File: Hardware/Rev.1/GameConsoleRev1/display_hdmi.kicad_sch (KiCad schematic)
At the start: 11 parts, among them J7 HDMI_A

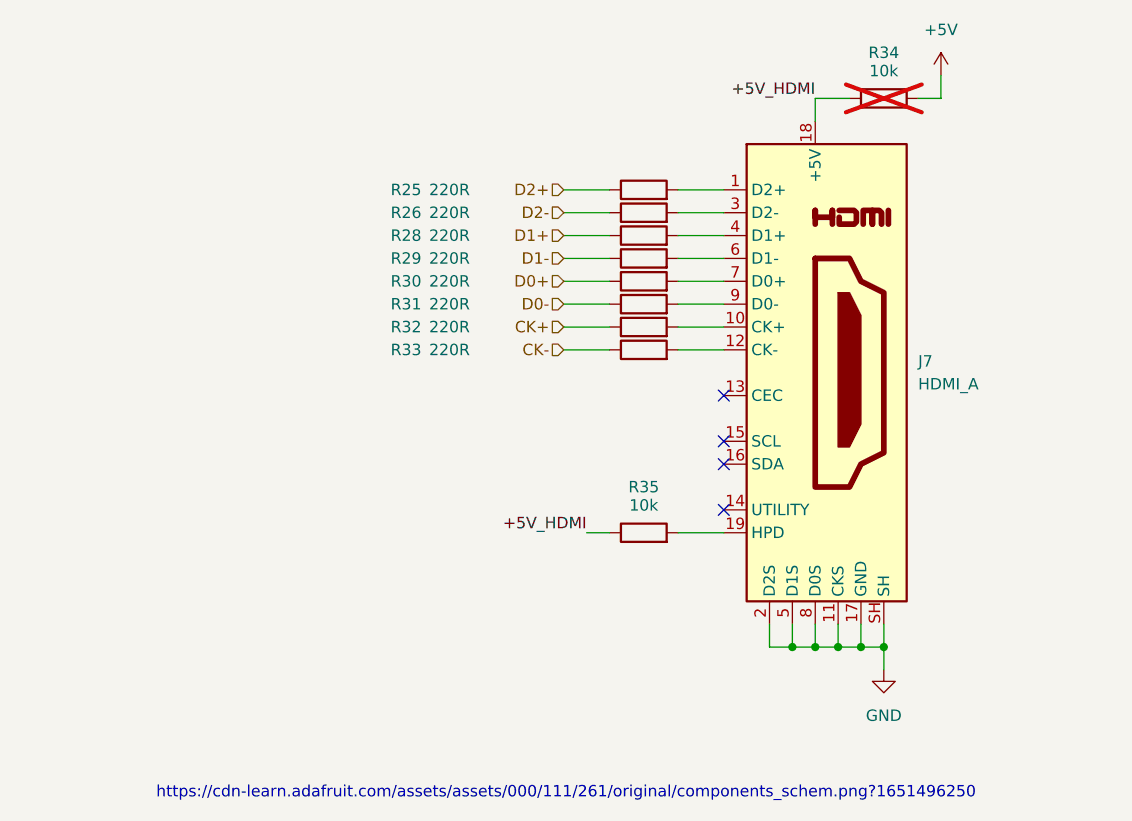
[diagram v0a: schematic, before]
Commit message: Added CPP Build
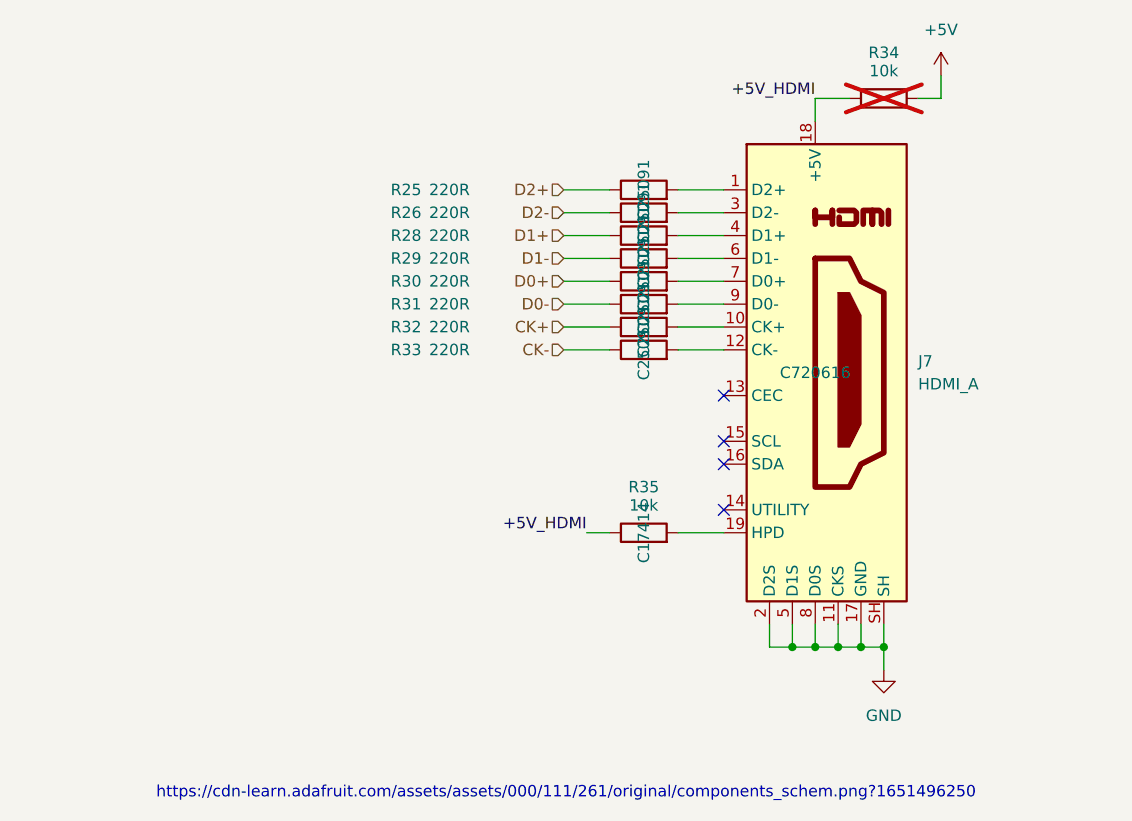
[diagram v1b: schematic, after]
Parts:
- J7: LCSC (none) -> C720616
- R25, R26, R28, R29, R30, R31, R32, R33: LCSC (none) -> C25091
- R35: LCSC (none) -> C17414
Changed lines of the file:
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@@
+			)
+		)
+		(property "DK" ""
+			(at 140.97 53.34 0)
+			(effects
+				(font
+					(size 1.27 1.27)
+				)
 			)
 		)
@@
 			)
 		)
+		(property "DK" ""
+			(at 114.3 71.12 0)
+			(effects
+				(font
+					(size 1.27 1.27)
+				)
+			)
+		)
+		(property "LCSC" "C25091"
+			(at 114.3 71.12 0)
+			(effects
+				(font
+					(size 1.27 1.27)
+				)
+			)
+		)
 		(pin "1"
 		)
@@
 			)
 		)
+		(property "DK" ""
+			(at 114.3 68.58 0)
+			(effects
+				(font
+					(size 1.27 1.27)
+				)
+			)
+		)
+		(property "LCSC" "C25091"
+			(at 114.3 68.58 0)
+			(effects
+				(font
+					(size 1.27 1.27)
+				)
+			)
+		)
 		(pin "1"
 		)
@@
 			)
 		)
+		(property "DK" ""
+			(at 114.3 66.04 0)
+			(effects
+				(font
+					(size 1.27 1.27)
+				)
+			)
+		)
+		(property "LCSC" "C25091"
+			(at 114.3 66.04 0)
+			(effects
+				(font
+					(size 1.27 1.27)
+				)
+			)
+		)
 		(pin "1"
 		)
@@
 			)
 		)
+		(property "DK" ""
+			(at 114.3 81.28 0)
+			(effects
+				(font
+					(size 1.27 1.27)
+				)
+			)
+		)
+		(property "LCSC" "C25091"
+			(at 114.3 81.28 0)
+			(effects
+				(font
+					(size 1.27 1.27)
+				)
+			)
+		)
 		(pin "1"
 		)
@@
 				)
 				(hide yes)
+			)
+		)
+		(property "DK" ""
+			(at 114.3 101.6 0)
+			(effects
+				(font
+					(size 1.27 1.27)
+				)
+			)
+		)
+		(property "LCSC" "C17414"
+			(at 114.3 101.6 0)
+			(effects
+				(font
+					(size 1.27 1.27)
+				)
 			)
 		)
@@
 			)
 		)
+		(property "DK" ""
+			(at 114.3 73.66 0)
+			(effects
+				(font
+					(size 1.27 1.27)
+				)
+			)
+		)
+		(property "LCSC" "C25091"
+			(at 114.3 73.66 0)
+			(effects
+				(font
+					(size 1.27 1.27)
+				)
+			)
+		)
 		(pin "1"
 		)
@@
 				)
 				(hide yes)
+			)
+		)
+		(property "DK" ""
+			(at 114.3 63.5 0)
+			(effects
+				(font
+					(size 1.27 1.27)
+				)
+			)
+		)
+		(property "LCSC" "C25091"
+			(at 114.3 63.5 0)
+			(effects
+				(font
+					(size 1.27 1.27)
+				)
 			)
 		)
@@
 			)
 		)
+		(property "LCSC" "C720616"
+			(at 133.35 83.82 0)
+			(effects
+				(font
+					(size 1.27 1.27)
+				)
+			)
+		)
+		(property "DK" ""
+			(at 133.35 83.82 0)
+			(effects
+				(font
+					(size 1.27 1.27)
+				)
+			)
+		)
 		(pin "3"
 		)
@@
 			)
 		)
+		(property "DK" ""
+			(at 114.3 76.2 0)
+			(effects
+				(font
+					(size 1.27 1.27)
+				)
+			)
+		)
+		(property "LCSC" "C25091"
+			(at 114.3 76.2 0)
+			(effects
+				(font
+					(size 1.27 1.27)
+				)
+			)
+		)
 		(pin "1"
 		)
@@
 			)
 		)
+		(property "DK" ""
+			(at 114.3 78.74 0)
+			(effects
+				(font
+					(size 1.27 1.27)
+				)
+			)
+		)
+		(property "LCSC" "C25091"
+			(at 114.3 78.74 0)
+			(effects
+				(font
+					(size 1.27 1.27)
+				)
+			)
+		)
